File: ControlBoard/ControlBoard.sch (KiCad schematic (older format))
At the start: 92 parts, among them J1 PowerIn, J10 Conn_01x01, J11 Conn_01x01, J19 HALLSENS, J2 UART, J20 Conn_01x06, J21 HALLSENS2, J22 PowerIn, J3 ICSP, J4 MTR1, J5 MTR2, J8 Conn_01x01, J9 Conn_01x01, Q1 2N3904, SW1 SW_Push, U1 LM358, U5 ATMEGA328P-PU, U6 LM7805_TO220, U7 74HC595, U8 L298D, U9 74HC595, Y1 16MHz

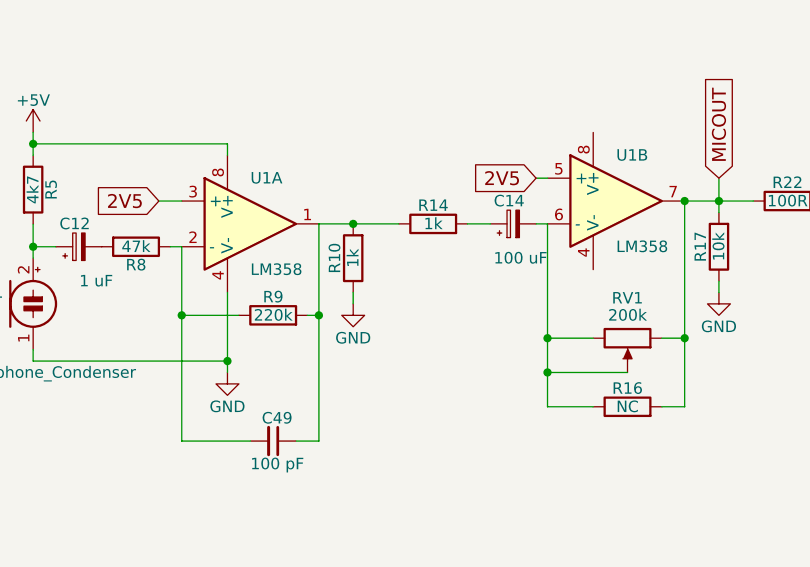
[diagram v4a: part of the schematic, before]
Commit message: Added some filter capacitors
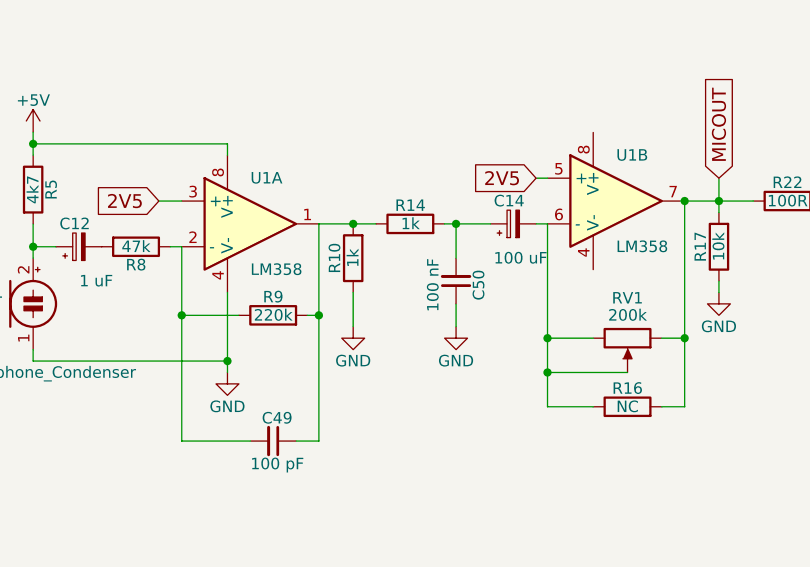
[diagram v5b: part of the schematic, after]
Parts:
- added C50: 100 nF, Capacitors_THT:C_Disc_D5.0mm_W2.5mm_P5.00mm, symbol C_Small
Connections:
- net GND: now also C50.1
- net at C14.1, R14.2: now also C50.2
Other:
- moved on the sheet: R14
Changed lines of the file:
@@
 $EndComp
 $Comp
-L GND #PWR53
+L GND #PWR54
 U 1 1 6146DC53
 P 10650 1800
-F 0 "#PWR53" H 10650 1550 50  0001 C CNN
+F 0 "#PWR54" H 10650 1550 50  0001 C CNN
 F 1 "GND" H 10650 1650 50  0000 C CNN
 F 2 "" H 10650 1800 50  0001 C CNN
@@
 LATCH
 $Comp
-L GND #PWR37
+L GND #PWR38
 U 1 1 6146F01B
 P 7750 1600
-F 0 "#PWR37" H 7750 1350 50  0001 C CNN
+F 0 "#PWR38" H 7750 1350 50  0001 C CNN
 F 1 "GND" H 7750 1450 50  0000 C CNN
 F 2 "" H 7750 1600 50  0001 C CNN
@@
 $EndComp
 $Comp
-L GND #PWR39
+L GND #PWR40
 U 1 1 6146F1BE
 P 8150 1950
-F 0 "#PWR39" H 8150 1700 50  0001 C CNN
+F 0 "#PWR40" H 8150 1700 50  0001 C CNN
 F 1 "GND" H 8150 1800 50  0000 C CNN
 F 2 "" H 8150 1950 50  0001 C CNN
@@
 $EndComp
 $Comp
-L +5V #PWR38
+L +5V #PWR39
 U 1 1 6146F30A
 P 8150 850
-F 0 "#PWR38" H 8150 700 50  0001 C CNN
+F 0 "#PWR39" H 8150 700 50  0001 C CNN
 F 1 "+5V" H 8150 990 50  0000 C CNN
 F 2 "" H 8150 850 50  0001 C CNN
@@
 MTRIN4
 $Comp
-L GND #PWR35
+L GND #PWR36
 U 1 1 6147450E
 P 7450 4050
-F 0 "#PWR35" H 7450 3800 50  0001 C CNN
+F 0 "#PWR36" H 7450 3800 50  0001 C CNN
 F 1 "GND" H 7450 3900 50  0000 C CNN
 F 2 "" H 7450 4050 50  0001 C CNN
@@
 $EndComp
 $Comp
-L +12V #PWR41
+L +12V #PWR42
 U 1 1 614757C0
 P 8400 2600
-F 0 "#PWR41" H 8400 2450 50  0001 C CNN
+F 0 "#PWR42" H 8400 2450 50  0001 C CNN
 F 1 "+12V" H 8400 2740 50  0000 C CNN
 F 2 "" H 8400 2600 50  0001 C CNN
@@
 $EndComp
 $Comp
-L GND #PWR45
+L GND #PWR46
 U 1 1 61475E0A
 P 9150 3450
-F 0 "#PWR45" H 9150 3200 50  0001 C CNN
+F 0 "#PWR46" H 9150 3200 50  0001 C CNN
 F 1 "GND" H 9150 3300 50  0000 C CNN
 F 2 "" H 9150 3450 50  0001 C CNN
@@
 $EndComp
 $Comp
-L +12V #PWR42
+L +12V #PWR43
 U 1 1 61476578
 P 8550 3650
-F 0 "#PWR42" H 8550 3500 50  0001 C CNN
+F 0 "#PWR43" H 8550 3500 50  0001 C CNN
 F 1 "+12V" H 8550 3790 50  0000 C CNN
 F 2 "" H 8550 3650 50  0001 C CNN
@@
 $EndComp
 $Comp
-L GND #PWR46
+L GND #PWR47
 U 1 1 614773C2
 P 9150 4500
-F 0 "#PWR46" H 9150 4250 50  0001 C CNN
+F 0 "#PWR47" H 9150 4250 50  0001 C CNN
 F 1 "GND" H 9150 4350 50  0000 C CNN
 F 2 "" H 9150 4500 50  0001 C CNN
@@
 L GND #PWR28
 U 1 1 6149A1B6
-P 5750 5950
-F 0 "#PWR28" H 5750 5700 50  0001 C CNN
-F 1 "GND" H 5750 5800 50  0000 C CNN
-F 2 "" H 5750 5950 50  0001 C CNN
-F 3 "" H 5750 5950 50  0001 C CNN
-	1    5750 5950
+P 5750 6050
+F 0 "#PWR28" H 5750 5800 50  0001 C CNN
+F 1 "GND" H 5750 5900 50  0000 C CNN
+F 2 "" H 5750 6050 50  0001 C CNN
+F 3 "" H 5750 6050 50  0001 C CNN
+	1    5750 6050
 	1    0    0    -1
 $EndComp
@@
 $EndComp
 $Comp
-L GND #PWR34
+L GND #PWR35
 U 1 1 6149A6CD
 P 7350 5900
-F 0 "#PWR34" H 7350 5650 50  0001 C CNN
+F 0 "#PWR35" H 7350 5650 50  0001 C CNN
 F 1 "GND" H 7350 5750 50  0000 C CNN
 F 2 "" H 7350 5900 50  0001 C CNN
@@
 $EndComp
 $Comp
-L GND #PWR40
+L GND #PWR41
 U 1 1 6149C645
 P 8300 5900
-F 0 "#PWR40" H 8300 5650 50  0001 C CNN
+F 0 "#PWR41" H 8300 5650 50  0001 C CNN
 F 1 "GND" H 8300 5750 50  0000 C CNN
 F 2 "" H 8300 5900 50  0001 C CNN
@@
 $EndComp
 $Comp
-L GND #PWR43
+L GND #PWR44
 U 1 1 6149CE43
 P 8700 5900
-F 0 "#PWR43" H 8700 5650 50  0001 C CNN
+F 0 "#PWR44" H 8700 5650 50  0001 C CNN
 F 1 "GND" H 8700 5750 50  0000 C CNN
 F 2 "" H 8700 5900 50  0001 C CNN
@@
 $EndComp
 $Comp
-L GND #PWR44
+L GND #PWR45
 U 1 1 6149D55F
 P 8950 6250
-F 0 "#PWR44" H 8950 6000 50  0001 C CNN
+F 0 "#PWR45" H 8950 6000 50  0001 C CNN
 F 1 "GND" H 8950 6100 50  0000 C CNN
 F 2 "" H 8950 6250 50  0001 C CNN
@@
 L R R14
 U 1 1 614AC6C4
-P 6100 5600
-F 0 "R14" V 6180 5600 50  0000 C CNN
-F 1 "1k" V 6100 5600 50  0000 C CNN
-F 2 "Resistors_THT:R_Axial_DIN0207_L6.3mm_D2.5mm_P7.62mm_Horizontal" V 6030 5600 50  0001 C CNN
-F 3 "" H 6100 5600 50  0001 C CNN
-	1    6100 5600
+P 6000 5600
+F 0 "R14" V 6080 5600 50  0000 C CNN
+F 1 "1k" V 6000 5600 50  0000 C CNN
+F 2 "Resistors_THT:R_Axial_DIN0207_L6.3mm_D2.5mm_P7.62mm_Horizontal" V 5930 5600 50  0001 C CNN
+F 3 "" H 6000 5600 50  0001 C CNN
+	1    6000 5600
 	0    -1   -1   0
 $EndComp
@@
 $EndComp
 $Comp
-L GND #PWR48
+L GND #PWR49
 U 1 1 614B9DA1
 P 9400 6250
-F 0 "#PWR48" H 9400 6000 50  0001 C CNN
+F 0 "#PWR49" H 9400 6000 50  0001 C CNN
 F 1 "GND" H 9400 6100 50  0000 C CNN
 F 2 "" H 9400 6250 50  0001 C CNN
@@
 $EndComp
 $Comp
-L +5V #PWR47
+L +5V #PWR48
 U 1 1 614BA2B8
 P 9400 5150
-F 0 "#PWR47" H 9400 5000 50  0001 C CNN
+F 0 "#PWR48" H 9400 5000 50  0001 C CNN
 F 1 "+5V" H 9400 5290 50  0000 C CNN
 F 2 "" H 9400 5150 50  0001 C CNN
@@
 	1800 5600 1950 5600
 Wire Wire Line
-	6350 5600 6250 5600
+	6150 5600 6350 5600
 Connection ~ 4750 1250
 Wire Wire Line
@@
 	6600 5400 6550 5400
 Wire Wire Line
-	5600 5600 5950 5600
+	5600 5600 5850 5600
 Wire Wire Line
 	5000 5700 5000 6550
@@
 	7200 5500 7500 5500
 Wire Wire Line
-	5750 5950 5750 5900
+	5750 6050 5750 5900
 Connection ~ 7200 5500
 Connection ~ 5200 6200
@@
 Connection ~ 3950 3850
 $Comp
-L GND #PWR36
+L GND #PWR37
 U 1 1 614E17CF
 P 7700 2050
-F 0 "#PWR36" H 7700 1800 50  0001 C CNN
+F 0 "#PWR37" H 7700 1800 50  0001 C CNN
 F 1 "GND" H 7700 1900 50  0000 C CNN
 F 2 "" H 7700 2050 50  0001 C CNN
@@
 	7700 2000 7700 2050
 $Comp
-L +5V #PWR33
+L +5V #PWR34
 U 1 1 614E1A8D
 P 6950 1850
-F 0 "#PWR33" H 6950 1700 50  0001 C CNN
+F 0 "#PWR34" H 6950 1700 50  0001 C CNN
 F 1 "+5V" H 6950 1990 50  0000 C CNN
 F 2 "" H 6950 1850 50  0001 C CNN
@@
 Connection ~ 10650 1500
 $Comp
-L +5V #PWR52
+L +5V #PWR53
 U 1 1 614E555C
 P 10650 1000
-F 0 "#PWR52" H 10650 850 50  0001 C CNN
+F 0 "#PWR53" H 10650 850 50  0001 C CNN
 F 1 "+5V" H 10650 1140 50  0000 C CNN
 F 2 "" H 10650 1000 50  0001 C CNN
@@
 $EndComp
 $Comp
-L GND #PWR50
+L GND #PWR51
 U 1 1 61523138
 P 10100 3550
-F 0 "#PWR50" H 10100 3300 50  0001 C CNN
+F 0 "#PWR51" H 10100 3300 50  0001 C CNN
 F 1 "GND" H 10100 3400 50  0000 C CNN
 F 2 "" H 10100 3550 50  0001 C CNN
@@
 	10100 3350 10000 3350
 $Comp
-L +5V #PWR49
+L +5V #PWR50
 U 1 1 61523719
 P 10100 3050
-F 0 "#PWR49" H 10100 2900 50  0001 C CNN
+F 0 "#PWR50" H 10100 2900 50  0001 C CNN
 F 1 "+5V" H 10100 3190 50  0000 C CNN
 F 2 "" H 10100 3050 50  0001 C CNN
@@
 Connection ~ 10100 3250
 $Comp
-L GND #PWR51
+L GND #PWR52
 U 1 1 61524424
 P 10400 3550
-F 0 "#PWR51" H 10400 3300 50  0001 C CNN
+F 0 "#PWR52" H 10400 3300 50  0001 C CNN
 F 1 "GND" H 10400 3400 50  0000 C CNN
 F 2 "" H 10400 3550 50  0001 C CNN
@@
 	5000 6550 5300 6550
 Connection ~ 5000 6000
+$Comp
+L C_Small C50
+U 1 1 61DD473D
+P 6200 5850
+F 0 "C50" V 6100 5800 50  0000 L CNN
+F 1 "100 nF" V 6300 5750 50  0000 L CNN
+F 2 "Capacitors_THT:C_Disc_D5.0mm_W2.5mm_P5.00mm" H 6200 5850 50  0001 C CNN
+F 3 "" H 6200 5850 50  0001 C CNN
+	1    6200 5850
+	-1   0    0    1
+$EndComp
+Wire Wire Line
+	6200 5750 6200 5600
+Connection ~ 6200 5600
+$Comp
+L GND #PWR33
+U 1 1 61DD4D29
+P 6200 6050
+F 0 "#PWR33" H 6200 5800 50  0001 C CNN
+F 1 "GND" H 6200 5900 50  0000 C CNN
+F 2 "" H 6200 6050 50  0001 C CNN
+F 3 "" H 6200 6050 50  0001 C CNN
+	1    6200 6050
+	1    0    0    -1
+$EndComp
+Wire Wire Line
+	6200 6050 6200 5950
 $EndSCHEMATC

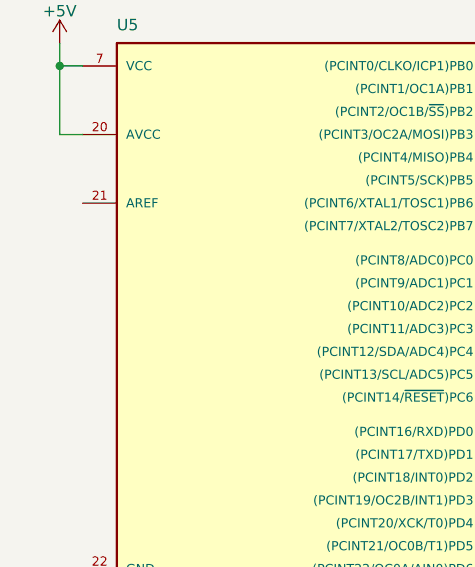
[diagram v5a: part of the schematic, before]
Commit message: Added capacitor for AREF
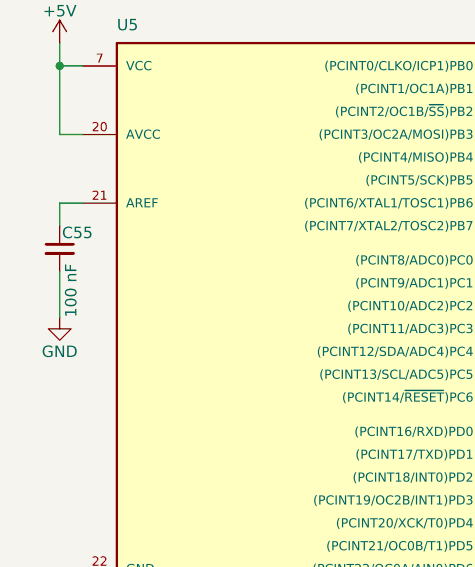
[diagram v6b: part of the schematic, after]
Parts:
- added C55: 100 nF, Capacitors_THT:C_Disc_D5.0mm_W2.5mm_P2.50mm, symbol C_Small
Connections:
- net GND: now also C55.2
- net at U5.21 (AREF): now also C55.1
